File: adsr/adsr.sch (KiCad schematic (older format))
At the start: 22 parts

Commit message: component selection
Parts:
- added C?: 100n, symbol Device:C
- added D?: D, symbol Device:D
- added Q? (x2): 2N3904, Package_TO_SOT_THT:TO-92_Inline, symbol Transistor_BJT:2N3904
- added R?: 1K, symbol Device:R
- added R? (x2): 100K, symbol Device:R
- added RV?: R_SUSTAIN, symbol Device:R_POT
- added U?: LM13700, symbol Amplifier_Operational:LM13700
- C1: renamed from C?; value 100u -> 22u
- R?: value 24K -> 12K
- RV?: value R_POT -> R_RELEASE
- RV?: value R_POT -> R_ATTACK
- RV?: value R_POT -> R_DECAY
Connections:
- net +12V: now also R?.1
- net +5V: now also J?.11 (5V)
- net A_GATE: now also U?.15 (IN1), U?.15 (IN1), R?.1
- net A_IN: now also RV?.1
- net GND: now also C?.2, Q?.1 (E), Q?.1 (E), RV?.3
- net A_STATE: now reaches U?.10 (IN2)
- net A_STATE: now also U?.10 (IN2), C?.1, D?.2 (A), U?.9
- net at U?.1: now also U?.10
- net A_S: no longer names the net of U?.6 (D4)
- net A_S: now also RV?.2
- new net: D?.1 (K), Q?.3 (C)
- new net: Q?.2 (B), R?.1
- new net: Q?.3 (C), R?.2, R?.2
- new net: Q?.2 (B), R?.2
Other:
- note added: "Choice of C1 and R_POT control the slew rate\nLarge values for both mean a longer charge time,\nbut a large C1 effects the fastest charge time too,\nsince IABC has a max of 2mA\n\nC1=22u, R_POT=500K gives a 0-5V charge time\nrange of 70ms to 2.7s"
- note added: "Limit IABC to 2mA"
- note added: "State machine controlled by STATE and GATE:\nAttack - Vgate=5, Vref=Vin, Iabc controlled by Rattack\nDecay - Vgate=5, Vref=Vsustain, Iabc controlled by Rdecay\nRelease - Vgate=0, Vref=0, Iabc controlled by Rrelease\n"
- note added: "cheap analog latch\nCapacitor is charged for D and S states,\ndischarged for A and R states"
- note added: "output buffer"
- note removed: "Limit IABC to 1mA"

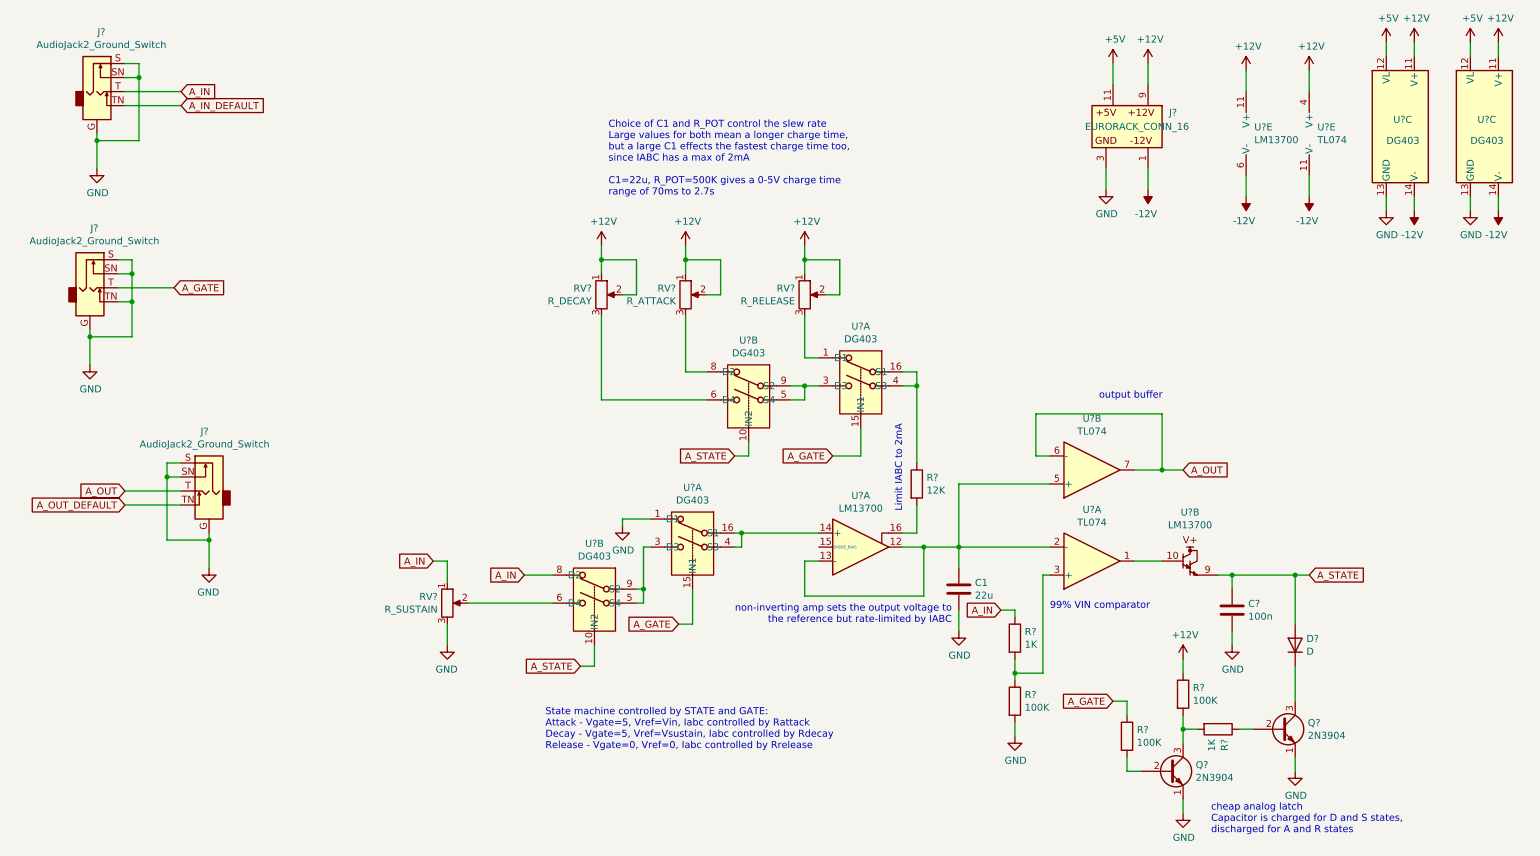
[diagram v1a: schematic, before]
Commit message: prepared pcb for dual envelopes
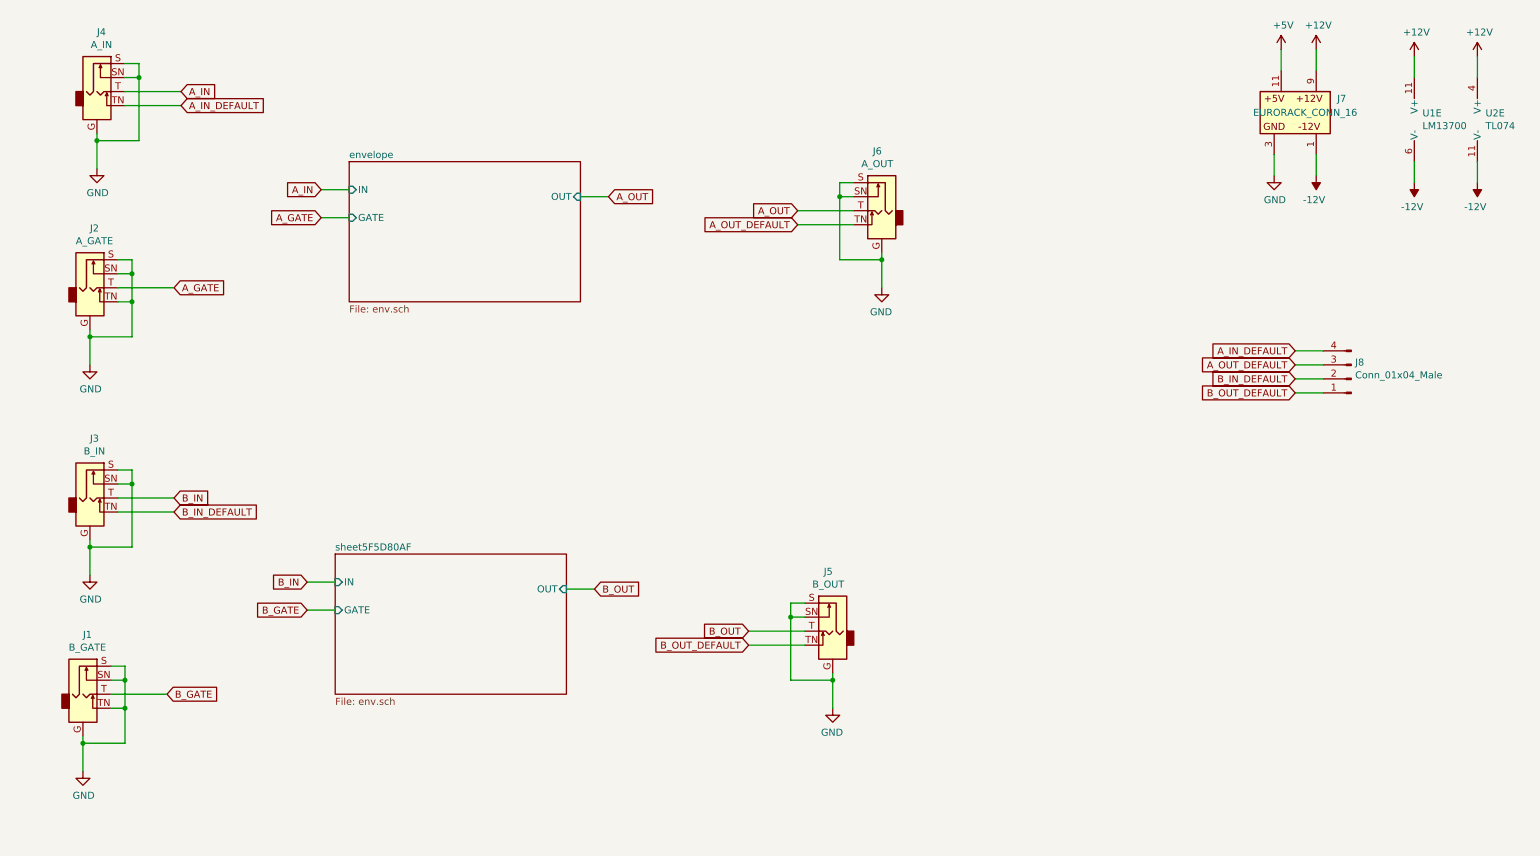
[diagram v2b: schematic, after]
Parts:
- removed C1: 22u, symbol Device:C
- removed C?: 100n, symbol Device:C
- removed D?: D, symbol Device:D
- removed Q? (x2): 2N3904, Package_TO_SOT_THT:TO-92_Inline, symbol Transistor_BJT:2N3904
- removed R?: 12K, symbol Device:R
- removed R? (x2): 1K, symbol Device:R
- removed R? (x3): 100K, symbol Device:R
- removed RV?: R_RELEASE, symbol Device:R_POT
- removed RV?: R_ATTACK, symbol Device:R_POT
- removed RV?: R_DECAY, symbol Device:R_POT
- removed RV?: R_SUSTAIN, symbol Device:R_POT
- removed U? (x2): LM13700, symbol Amplifier_Operational:LM13700
- removed U? (x6): DG403, Package_SO:SOIC-16_3.9x9.9mm_P1.27mm, symbol synth:DG403
- removed U? (x2): TL074, symbol Amplifier_Operational:TL074
- added J1: B_GATE, synth:3.5MM_Jack_Breakout_Vertical, symbol synth:AudioJack2_Ground_Switch
- added J3: B_IN, synth:3.5MM_Jack_Breakout_Vertical, symbol synth:AudioJack2_Ground_Switch
- added J5: B_OUT, synth:3.5MM_Jack_Breakout_Vertical, symbol synth:AudioJack2_Ground_Switch
- added J8: Conn_01x04_Male, Connector_PinHeader_2.54mm:PinHeader_2x02_P2.54mm_Vertical, symbol Connector:Conn_01x04_Male
- J2: renamed from J?; value AudioJack2_Ground_Switch -> A_GATE
- J4: renamed from J?; value AudioJack2_Ground_Switch -> A_IN
- J6: renamed from J?; value AudioJack2_Ground_Switch -> A_OUT
- U1: renamed from U?; footprint (none) -> Package_DIP:DIP-16_W7.62mm
- U2: renamed from U?; footprint (none) -> Package_DIP:DIP-14_W7.62mm
- gave numbers to parts that had none: 1
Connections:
- net A_IN_DEFAULT: now also J8.4 (Pin_4)
- net A_OUT_DEFAULT: now also J8.3 (Pin_3)
- net GND: now also J1.G, J1.S, J1.SN, J1.TN, J3.G, J3.S, J3.SN, J5.G, J5.S, J5.SN
- new net B_GATE: J1.T
- new net B_IN: J3.T
- new net B_IN_DEFAULT: J3.TN, J8.2 (Pin_2)
- new net B_OUT: J5.T
- new net B_OUT_DEFAULT: J5.TN, J8.1 (Pin_1)
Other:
- note removed: "99% VIN comparator"
- note removed: "Choice of C1 and R_POT control the slew rate\nLarge values for both mean a longer charge time,\nbut a large C1 effects the fastest charge time too,\nsince IABC has a max of 2mA\n\nC1=22u, R_POT=500K gives a 0-5V charge time\nrange of 70ms to 2.7s"
- note removed: "Limit IABC to 2mA"
- note removed: "State machine controlled by STATE and GATE:\nAttack - Vgate=5, Vref=Vin, Iabc controlled by Rattack\nDecay - Vgate=5, Vref=Vsustain, Iabc controlled by Rdecay\nRelease - Vgate=0, Vref=0, Iabc controlled by Rrelease\n"
- note removed: "cheap analog latch\nCapacitor is charged for D and S states,\ndischarged for A and R states"
- note removed: "non-inverting amp sets the output voltage to\nthe reference but rate-limited by IABC"
- note removed: "output buffer"
- moved on the sheet: J6, J7, U1E, U2E

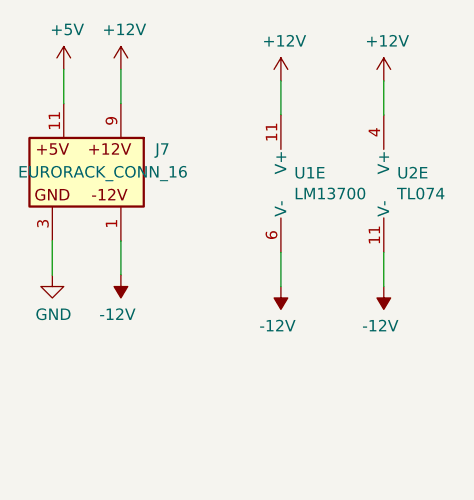
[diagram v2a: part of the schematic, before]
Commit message: use a current mirror to isolate reference currents, buffer vin, tune params
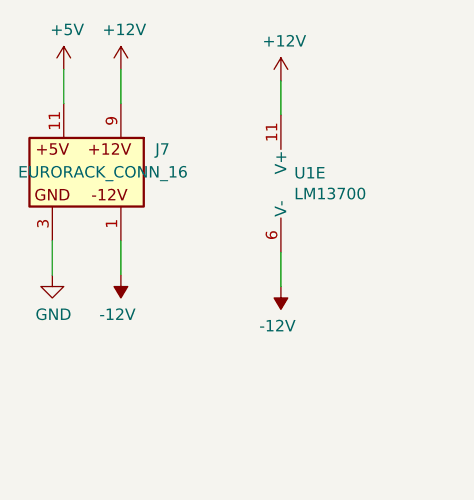
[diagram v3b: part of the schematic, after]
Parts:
- removed U2: TL074, Package_DIP:DIP-14_W7.62mm, symbol Amplifier_Operational:TL074
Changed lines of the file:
@@
 	10400 1000 10400 850
-$Comp
-L Amplifier_Operational:TL074 U2
-U 5 1 5F2A4C99
-P 10950 1300
-F 0 "U2" H 10908 1346 50  0000 L CNN
-F 1 "TL074" H 10908 1255 50  0000 L CNN
-F 2 "Package_DIP:DIP-14_W7.62mm" H 10900 1400 50  0001 C CNN
-F 3 "http://www.ti.com/lit/ds/symlink/tl071.pdf" H 11000 1500 50  0001 C CNN
-	5    10950 1300
-	1    0    0    -1
-$EndComp
 $Comp
 L synth:AudioJack2_Ground_Switch J4
@@
 Wire Wire Line
 	9400 1550 9400 1700
-Wire Wire Line
-	10850 1750 10850 1600
-Wire Wire Line
-	10850 850  10850 1000
-$Comp
-L power:-12V #PWR014
-U 1 1 5F3CA891
-P 10850 1750
-F 0 "#PWR014" H 10850 1850 50  0001 C CNN
-F 1 "-12V" H 10865 1923 50  0000 C CNN
-F 2 "" H 10850 1750 50  0001 C CNN
-F 3 "" H 10850 1750 50  0001 C CNN
-	1    10850 1750
-	-1   0    0    1
-$EndComp
-$Comp
-L power:+12V #PWR013
-U 1 1 5F3CBE19
-P 10850 850
-F 0 "#PWR013" H 10850 700 50  0001 C CNN
-F 1 "+12V" H 10865 1023 50  0000 C CNN
-F 2 "" H 10850 850 50  0001 C CNN
-F 3 "" H 10850 850 50  0001 C CNN
-	1    10850 850
-	1    0    0    -1
-$EndComp
 $Comp
 L power:+5V #PWR08

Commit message: rework ASDR
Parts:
- removed J1: B_GATE, synth:3.5MM_Jack_Breakout_Vertical, symbol synth:AudioJack2_Ground_Switch
- removed J2: A_GATE, synth:3.5MM_Jack_Breakout_Vertical, symbol synth:AudioJack2_Ground_Switch
- removed J3: B_IN, synth:3.5MM_Jack_Breakout_Vertical, symbol synth:AudioJack2_Ground_Switch
- removed J4: A_IN, synth:3.5MM_Jack_Breakout_Vertical, symbol synth:AudioJack2_Ground_Switch
- removed J5: B_OUT, synth:3.5MM_Jack_Breakout_Vertical, symbol synth:AudioJack2_Ground_Switch
- removed J6: A_OUT, synth:3.5MM_Jack_Breakout_Vertical, symbol synth:AudioJack2_Ground_Switch
- added C5, C6: 0.1u, Capacitor_SMD:C_1206_3216Metric_Pad1.42x1.75mm_HandSolder, symbol Device:C
- added J1: B_GATE, synth:Jack_3.5mm_QingPu_WQP-PJ398SM_Vertical_CircularHoles, symbol Connector:AudioJack2_SwitchT
- added J2: A_GATE, synth:Jack_3.5mm_QingPu_WQP-PJ398SM_Vertical_CircularHoles, symbol Connector:AudioJack2_SwitchT
- added J3: B_IN, synth:Jack_3.5mm_QingPu_WQP-PJ398SM_Vertical_CircularHoles, symbol Connector:AudioJack2_SwitchT
- added J4: A_IN, synth:Jack_3.5mm_QingPu_WQP-PJ398SM_Vertical_CircularHoles, symbol Connector:AudioJack2_SwitchT
- added J5: B_OUT, synth:Jack_3.5mm_QingPu_WQP-PJ398SM_Vertical_CircularHoles, symbol Connector:AudioJack2_SwitchT
- added J6: A_OUT, synth:Jack_3.5mm_QingPu_WQP-PJ398SM_Vertical_CircularHoles, symbol Connector:AudioJack2_SwitchT
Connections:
- net +12V: now also C5.1
- net -12V: now also C6.2
- net A_GATE: now also J2.T
- net A_IN: now also J4.T
- net A_IN_DEFAULT: now also J8.1 (Pin_1), J4.TN; no longer J8.4 (Pin_4)
- net A_OUT: now also J6.T
- net A_OUT_DEFAULT: now also J6.TN
- net B_GATE: now also J1.T
- net B_IN: now also J3.T
- net B_IN_DEFAULT: now also J3.TN
- net B_OUT: now also J5.T
- net B_OUT_DEFAULT: now also J8.4 (Pin_4), J5.TN; no longer J8.1 (Pin_1)
- net GND: now also C5.2, C6.1, J1.S, J1.TN, J2.S, J2.TN, J3.S, J4.S, J5.S, J6.S
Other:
- note added: "Bypass capacitors for LM13700"

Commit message: more layout
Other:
- note added: "TODO: IN and GATE are the same thing????"
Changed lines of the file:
@@
 Text Notes 7600 1850 0    50   ~ 0
 Bypass capacitors for LM13700
+Text Notes 2050 3100 0    50   ~ 0
+TODO: IN and GATE are the same thing????
 $EndSCHEMATC
